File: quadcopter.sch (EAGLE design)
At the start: 66 parts, among them J1 ISP, SW1 PUSHBUTTON_SMD-VERTICAL-1, U2 ATMEGA128RFA1

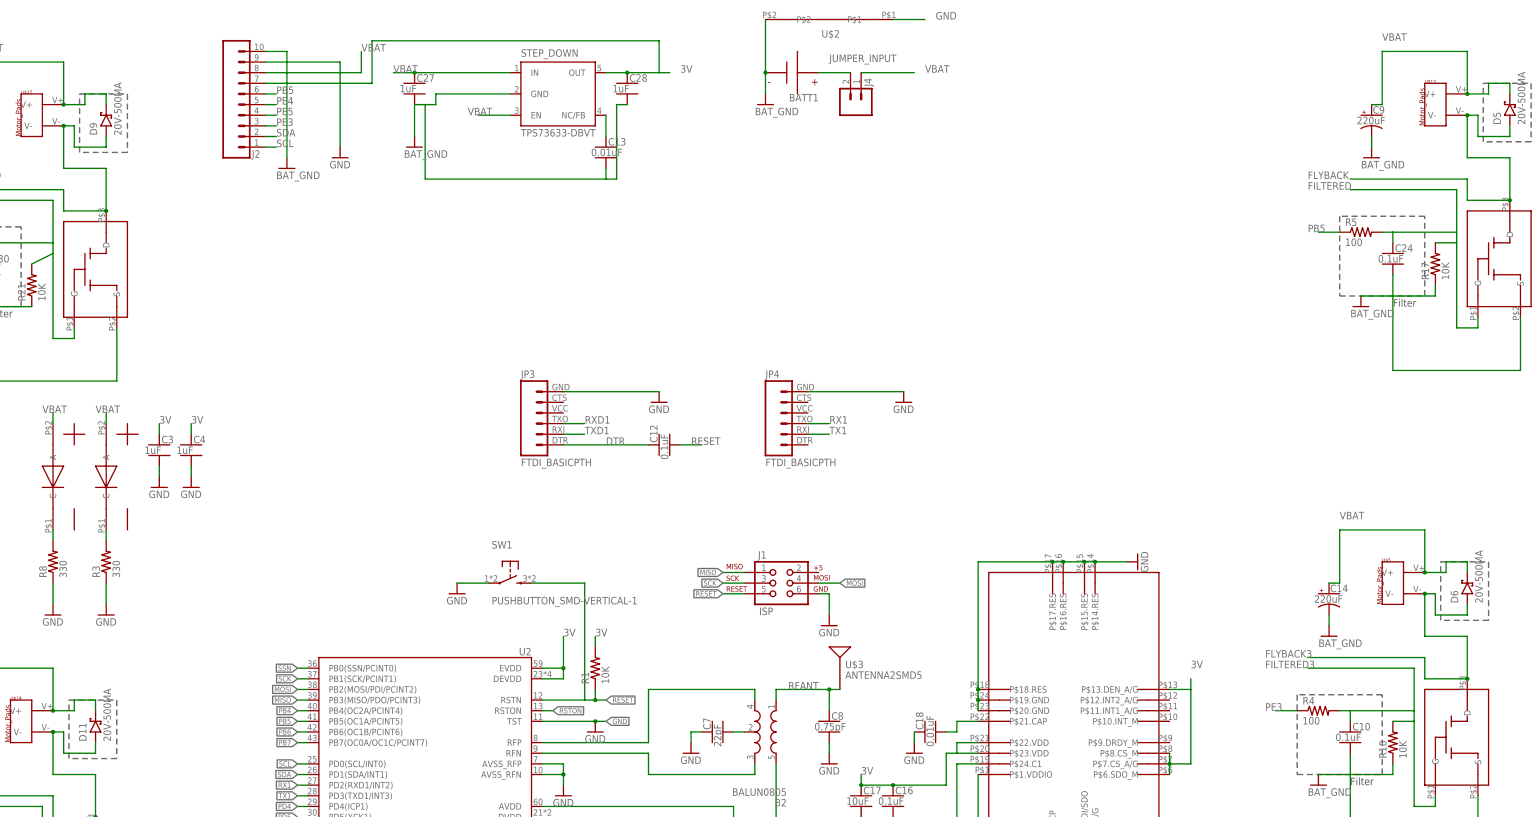
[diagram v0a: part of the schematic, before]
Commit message: bigger mosfet pads, no vias leading to oscillator, cap 28 and 13 (?) go to gnd instead of bat_gnd, made antenna better
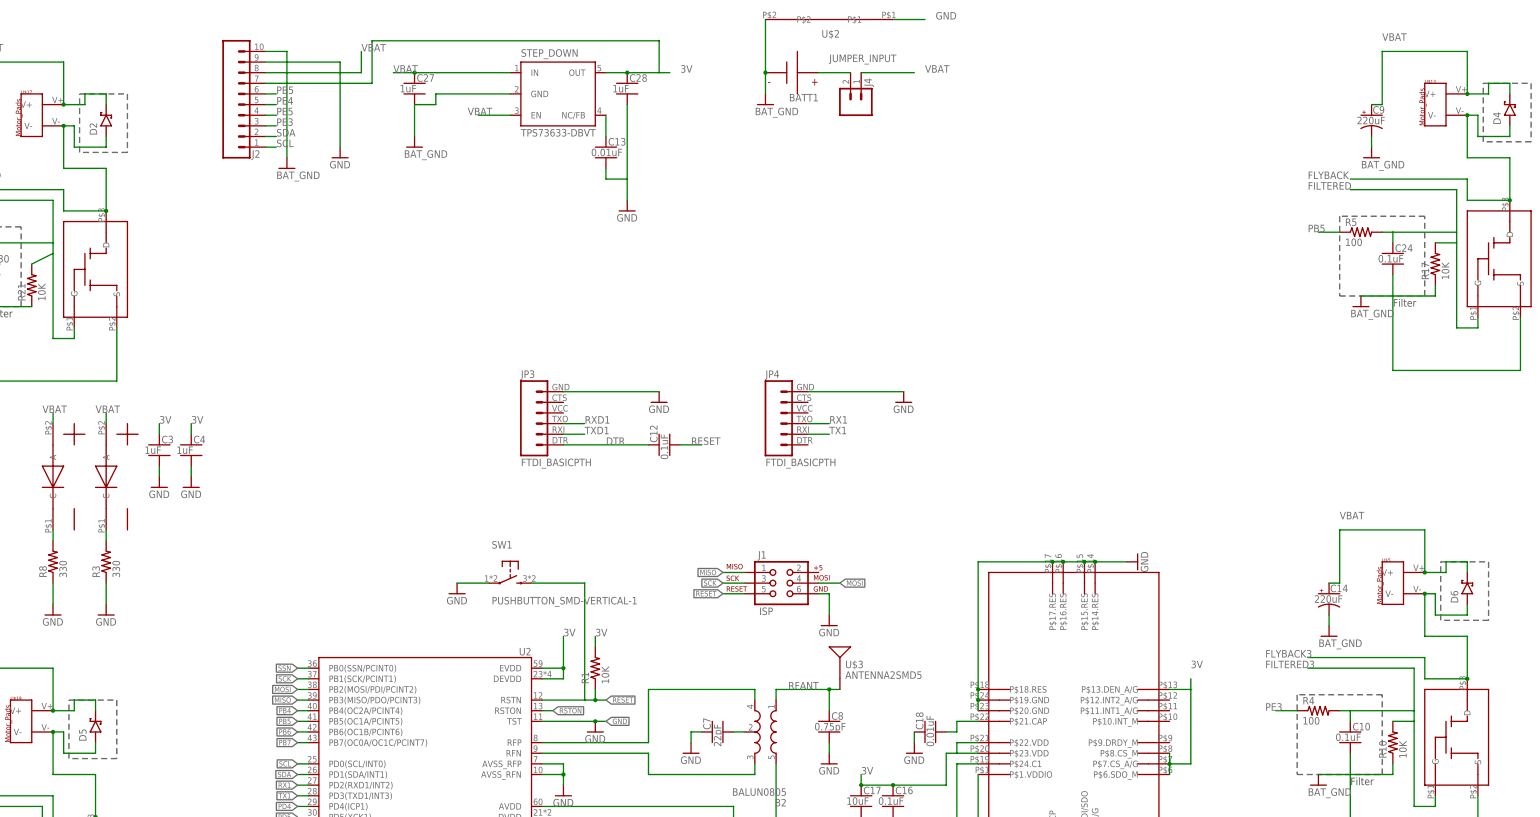
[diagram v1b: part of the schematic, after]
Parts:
- removed D11, D9: 20V-500MA, quadparts_prebuilt:DIODE-SCHOTTKY_SMD-SOD123-360MV
- added D2, D4: (no value), quadparts_prebuilt:DIODE-SCHOTTKY_SMD-SOD123
- D5, D6: value 20V-500MA -> (none); device quadparts_prebuilt:DIODE-SCHOTTKY_SMD-SOD123-360MV -> quadparts_prebuilt:DIODE-SCHOTTKY_SMD-SOD123
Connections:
- net BAT_GND: no longer C13.2, C28.2
- net FLYBACK: now also D4.A; no longer D5.A
- net FLYBACK1: now also D2.A; no longer D9.A
- net FLYBACK5: now also D5.A; no longer D11.A
- net GND: now also C13.2, C28.2
- net VBAT: now also D2.C, D4.C; no longer D11.C, D9.C
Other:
- moved on the sheet: D5

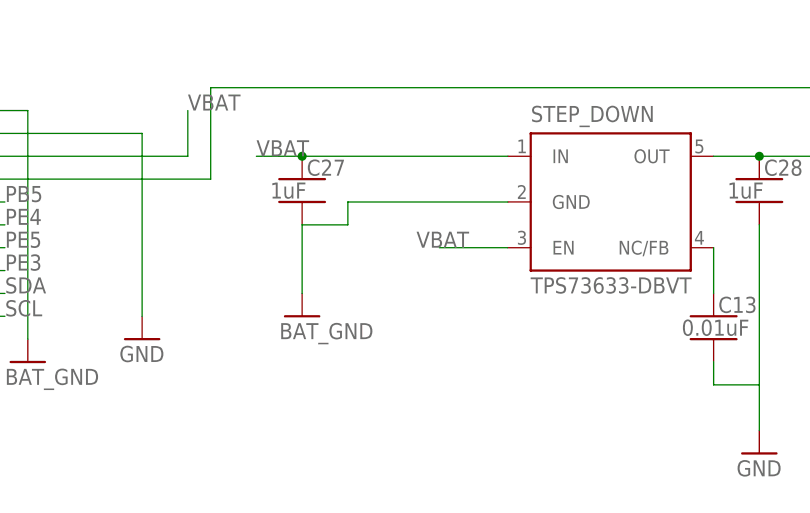
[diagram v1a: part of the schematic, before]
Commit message: changed most gnds on regulator to gnd instead of bat_gnd
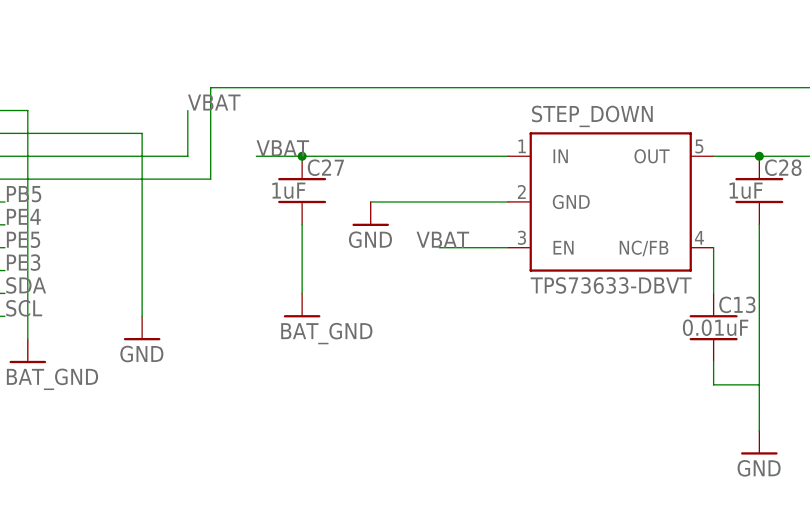
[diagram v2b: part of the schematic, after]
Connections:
- net BAT_GND: no longer STEP_DOWN.GND
- net GND: now also STEP_DOWN.GND
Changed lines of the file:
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@@
 <part name="D5" library="quadparts_prebuilt" deviceset="DIODE-SCHOTTKY_" device="SMD-SOD123"/>
 <part name="D6" library="quadparts_prebuilt" deviceset="DIODE-SCHOTTKY_" device="SMD-SOD123"/>
+<part name="GND32" library="quadparts_prebuilt" deviceset="GND" device=""/>
 </parts>
 <sheets>
@@
 <instance part="D5" gate="G$1" x="-68.58" y="0" rot="R90"/>
 <instance part="D6" gate="G$1" x="259.08" y="33.02" rot="R90"/>
+<instance part="GND32" gate="1" x="15.24" y="147.32"/>
 </instances>
 <busses>
@@
 <wire x1="53.34" y1="129.54" x2="58.42" y2="129.54" width="0.1524" layer="91"/>
 </segment>
+<segment>
+<pinref part="STEP_DOWN" gate="G$1" pin="GND"/>
+<pinref part="GND32" gate="1" pin="GND"/>
+<wire x1="30.48" y1="149.86" x2="15.24" y2="149.86" width="0.1524" layer="91"/>
+</segment>
 </net>
 <net name="N$3" class="0">
@@
 <wire x1="7.62" y1="139.7" x2="7.62" y2="147.32" width="0.1524" layer="91"/>
 <pinref part="GND25" gate="1" pin="BAT_GND"/>
-<pinref part="STEP_DOWN" gate="G$1" pin="GND"/>
-<wire x1="30.48" y1="149.86" x2="12.7" y2="149.86" width="0.1524" layer="91"/>
-<wire x1="12.7" y1="149.86" x2="12.7" y2="147.32" width="0.1524" layer="91"/>
-<wire x1="12.7" y1="147.32" x2="7.62" y2="147.32" width="0.1524" layer="91"/>
-</segment>
-<segment>
+</segment>
+<segment>
